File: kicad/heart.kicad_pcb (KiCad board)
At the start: 2 copper layers, 29.8 x 25.4 mm, 3 parts

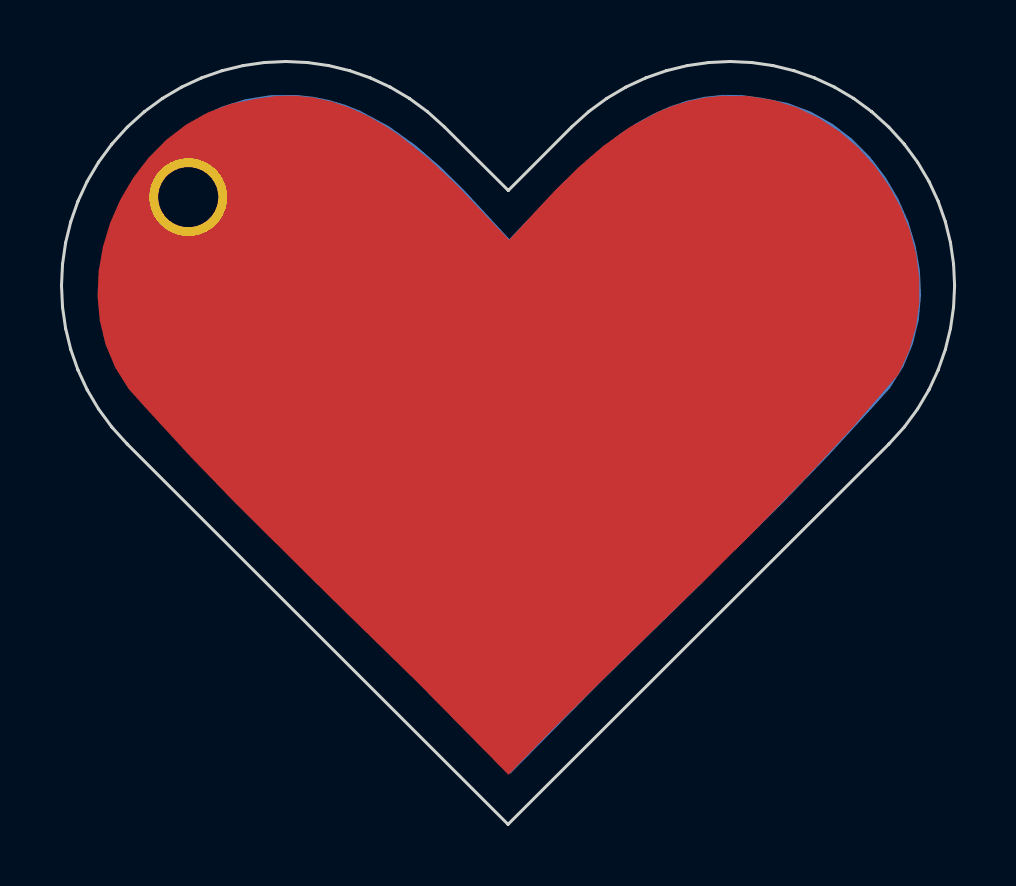
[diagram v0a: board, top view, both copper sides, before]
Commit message: slightly modify inner heart shape
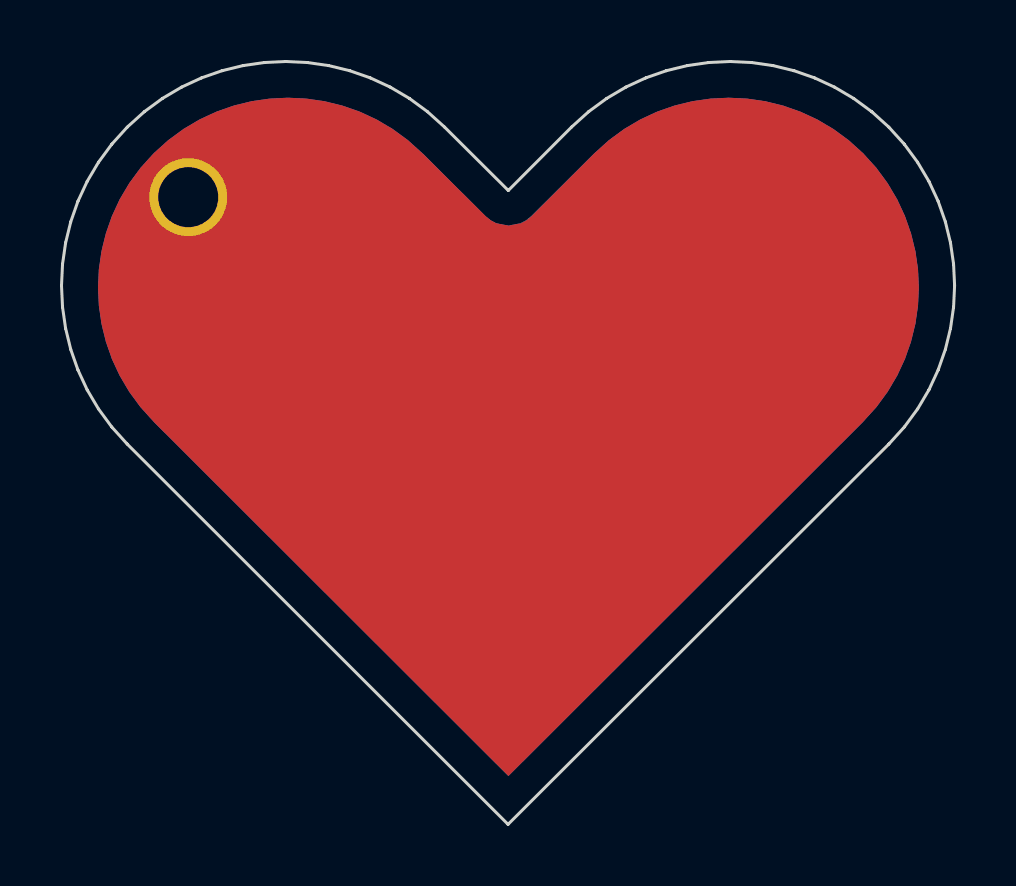
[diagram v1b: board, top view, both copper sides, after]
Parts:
- removed the svg2mod at (163.5, 92.0)
- removed the svg2mod at (163.4, 92.0)
- added svg2mod: G***, heart:heart, F.Cu at (163.4, 92.0)
- added svg2mod: G***, heart:heart, B.Cu at (163.4, 92.0)
